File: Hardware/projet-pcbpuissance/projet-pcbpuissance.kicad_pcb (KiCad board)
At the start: 2 copper layers, 61 x 61 mm, 32 parts, among them U1 MAX5033DUSA+, U2 MAX5033DUSA+

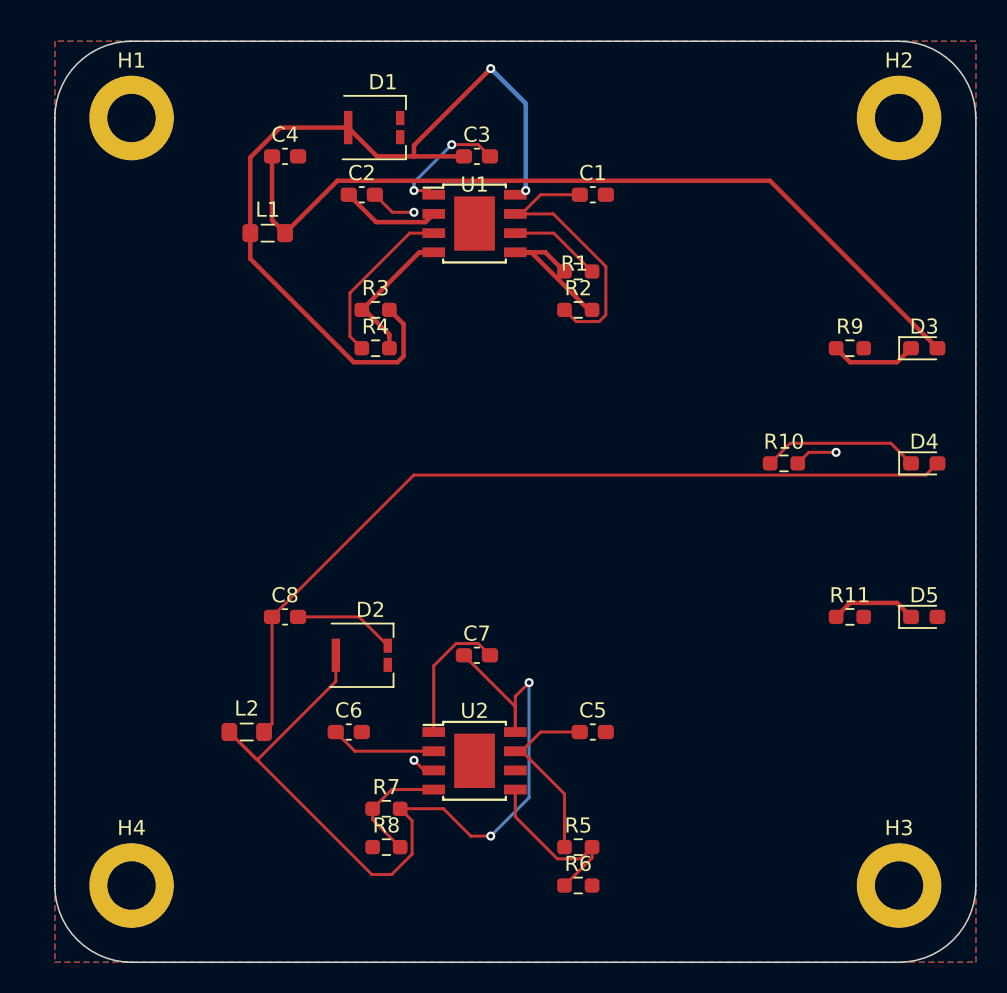
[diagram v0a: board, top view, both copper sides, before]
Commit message: Modification pcb-puissance
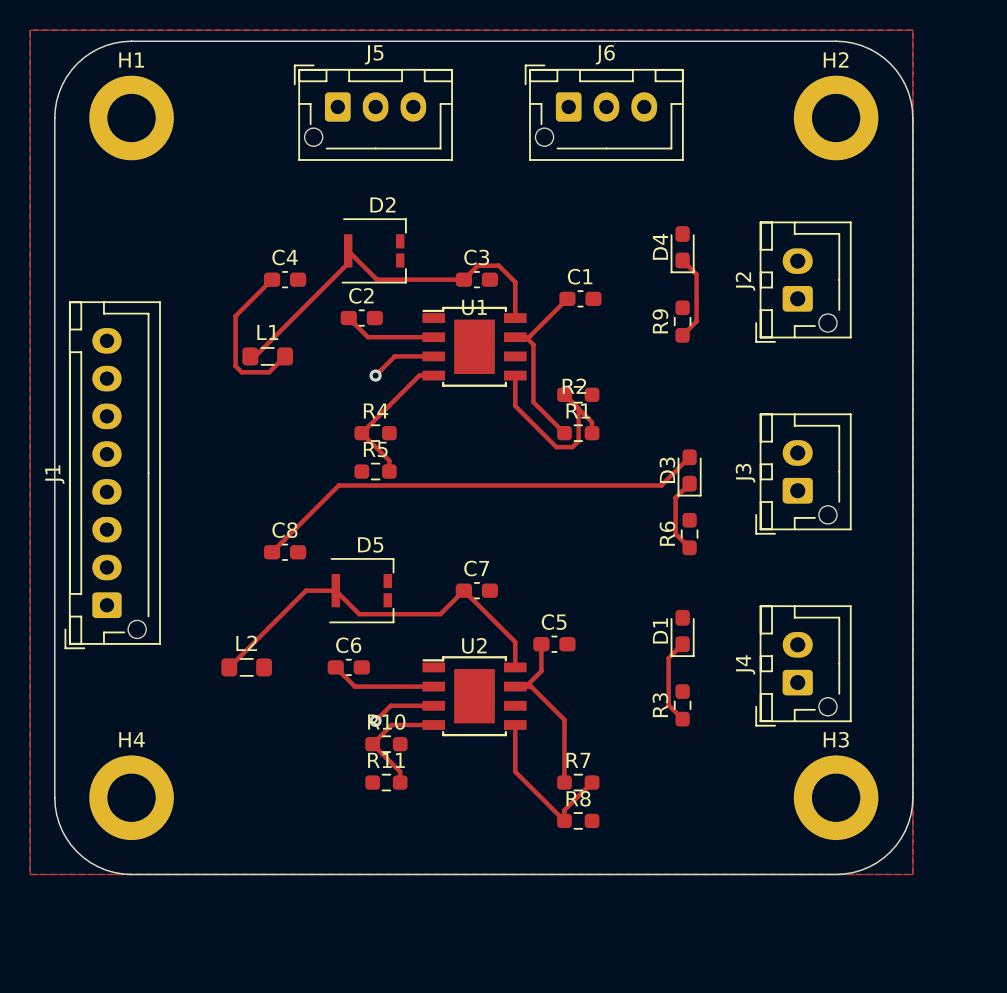
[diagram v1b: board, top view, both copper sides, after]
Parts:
- added J1: Conn_01x08, Connector_JST:JST_XH_B8B-XH-AM_1x08_P2.50mm_Vertical, F.Cu at (21.2, 60.2)
- added J2: Conn_01x02, Connector_JST:JST_XH_B2B-XH-AM_1x02_P2.50mm_Vertical, F.Cu at (67.0, 39.9)
- added J3: Conn_01x02, Connector_JST:JST_XH_B2B-XH-AM_1x02_P2.50mm_Vertical, F.Cu at (67.0, 52.6)
- added J4: Conn_01x02, Connector_JST:JST_XH_B2B-XH-AM_1x02_P2.50mm_Vertical, F.Cu at (67.0, 65.3)
- added J5: Conn_01x03, Connector_JST:JST_XH_B3B-XH-AM_1x03_P2.50mm_Vertical, F.Cu at (36.5, 27.2)
- added J6: Conn_01x03, Connector_JST:JST_XH_B3B-XH-AM_1x03_P2.50mm_Vertical, F.Cu at (51.8, 27.2)
- R1: renamed from R2; value 4,7M -> R_Small
- R2: renamed from R1; value 820k -> R_Small
- R7: renamed from R5; value 4,7M -> R_Small
- R8: renamed from R6; value 820k -> R_Small
- moved D4 29.2 mm to (59.3, 36.5), turned to 90 degrees
- moved R3 26.1 mm to (59.3, 66.8), turned to 90 degrees
- moved D1 24.6 mm to (59.3, 61.9), turned to 90 degrees
- moved R9 22.5 mm to (59.3, 41.4), turned to 90 degrees
- moved D3 15.5 mm to (59.8, 51.3), turned to 90 degrees
- moved R5 8.16 mm to (39.0, 51.3)
- moved U1 8.16 mm to (45.6, 43.1)
- moved C3 8.16 mm to (45.7, 38.6)
- moved C4 8.16 mm to (33.0, 38.6)
- moved D2 8.16 mm to (38.9, 36.7)
- moved C2 8.16 mm to (38.1, 41.2)
- moved L1 8.16 mm to (31.9, 43.7)
- moved R1 8.16 mm to (52.4, 48.8)
- moved R2 8.16 mm to (52.4, 46.3)
- moved R4 8.16 mm to (39.0, 48.8)
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- renumbered D3 to D1, D1 to D2, D4 to D3, D5 to D4, D2 to D5, R7 to R10, R8 to R11, R9 to R3, R3 to R4, R4 to R5, R10 to R6, R11 to R9
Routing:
- net +3.3V: track 54.6 -> 10.6 mm
- net Net-(D5-K): track 59.6 -> 25.4 mm, vias 2 -> 0
- net Net-(D2-K): track 57.3 -> 24.9 mm, vias 2 -> 0
- net 7.4V: track 56.1 -> 30.2 mm
- net GND: track 31.9 -> 8.64 mm, vias 3 -> 2
- net Net-(U2-BST): track 9.03 -> 0.00 mm
- net Net-(U1-BST): track 8.35 -> 0.00 mm, vias 2 -> 0
- net Batterie 11.1 V: track 31.4 -> 24.9 mm
- net Net-(D3-K): track 10.4 -> 5.01 mm
- net Net-(U1-ON/~{OFF}): track 10.4 -> 14.2 mm
- net Net-(U1-VD): track 7.38 -> 6.15 mm
- net Net-(U2-ON/~{OFF}): track 11.7 -> 11.0 mm
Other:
- board size 61 x 61 mm -> 56.8 x 55.2 mm

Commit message: Modif
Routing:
- net +3.3V: track 10.6 -> 47.3 mm, vias 0 -> 2
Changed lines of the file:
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@@
   (segment (start 59.3325 67.7275) (end 58.4075 66.8025) (width 0.3) (layer "F.Cu") (net 4))
   (segment (start 33.02 43.72) (end 31.97 44.77) (width 0.3) (layer "F.Cu") (net 6))
+  (segment (start 59.3325 61.02) (end 57.5825 61.02) (width 0.3) (layer "F.Cu") (net 6))
   (segment (start 30.155051 44.77) (end 29.745 44.359949) (width 0.3) (layer "F.Cu") (net 6))
   (segment (start 29.745 41.0525) (end 32.1575 38.64) (width 0.3) (layer "F.Cu") (net 6))
+  (segment (start 33.9325 50.07) (end 33.9325 44.6325) (width 0.3) (layer "F.Cu") (net 6))
+  (segment (start 57.5825 61.02) (end 51.7125 55.15) (width 0.3) (layer "F.Cu") (net 6))
   (segment (start 31.97 44.77) (end 30.155051 44.77) (width 0.3) (layer "F.Cu") (net 6))
+  (segment (start 33.9325 44.6325) (end 33.02 43.72) (width 0.3) (layer "F.Cu") (net 6))
   (segment (start 29.745 44.359949) (end 29.745 41.0525) (width 0.3) (layer "F.Cu") (net 6))
+  (via (at 33.9325 50.07) (size 0.8) (drill 0.4) (layers "F.Cu" "B.Cu") (net 6))
+  (via (at 51.7125 55.15) (size 0.8) (drill 0.4) (layers "F.Cu" "B.Cu") (net 6))
+  (segment (start 41.5525 55.15) (end 39.0125 55.15) (width 0.3) (layer "B.Cu") (net 6))
+  (segment (start 39.0125 55.15) (end 33.9325 50.07) (width 0.3) (layer "B.Cu") (net 6))
+  (segment (start 51.7125 55.15) (end 41.5525 55.15) (width 0.3) (layer "B.Cu") (net 6))
   (segment (start 36.375 64.305) (end 37.645 65.575) (width 0.3) (layer "F.Cu") (net 7))
   (segment (start 37.645 65.575) (end 42.86 65.575) (width 0.3) (layer "F.Cu") (net 7))

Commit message: Modification pcb puissance
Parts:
- removed J1: Conn_01x08, Connector_JST:JST_XH_B8B-XH-AM_1x08_P2.50mm_Vertical
- removed J5, J6: Conn_01x03, Connector_JST:JST_XH_B3B-XH-AM_1x03_P2.50mm_Vertical
- moved J2 18.3 mm to (51.7, 29.7), turned to 180 degrees
- moved H1 8.72 mm to (31.4, 29.8)
- moved H4 8.53 mm to (31.4, 72.9)
- moved J3 7.66 mm to (67.0, 45.0)
- moved H2 1.81 mm to (69.5, 29.8)
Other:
- board size 56.8 x 55.2 mm -> 48.3 x 53.3 mm

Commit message: Modif pcb-puissance
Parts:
- moved R6 26.5 mm to (33.9, 49.8)
- moved D3 26.4 mm to (33.9, 45.9)
- moved D4 16.5 mm to (67.0, 51.1)
- moved R9 16.5 mm to (67.0, 56.1)
- moved C1 7.38 mm to (59.4, 42.7)
- moved C2 7.38 mm to (44.9, 44.0)
- moved C3 7.38 mm to (52.5, 41.4)
- moved D2 7.38 mm to (45.7, 39.5)
- moved R1 7.38 mm to (59.3, 51.6)
- moved R2 7.38 mm to (59.3, 49.1)
- moved R4 7.38 mm to (45.8, 51.6)
- moved R5 7.38 mm to (45.8, 54.1)
- moved U1 7.38 mm to (52.4, 45.9)
- moved L1 7.38 mm to (38.7, 46.5)
- moved C4 7.38 mm to (39.8, 41.4)
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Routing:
- net Net-(D2-K): track 24.9 -> 44.8 mm, vias 0 -> 2
- net 7.4V: track 30.2 -> 21.3 mm
- net +3.3V: track 47.3 -> 41.6 mm
- net Net-(D5-K): track 25.4 -> 22.8 mm
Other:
- board size 48.3 x 53.3 mm -> 43.2 x 50.8 mm

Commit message: Modif pcb puissance
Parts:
- moved R9 27.4 mm to (53.3, 32.3), turned to 180 degrees
- moved D4 27.1 mm to (47.5, 32.3), turned to 180 degrees
- moved J2 18.9 mm to (67.0, 43.4), turned to 90 degrees
- moved J3 7.62 mm to (67.0, 52.6)
- moved D1 4.18 mm to (56.8, 58.6)
- moved R3 4.18 mm to (56.8, 63.5)
- moved J4 2.58 mm to (67.0, 62.7)
- moved H3 2.54 mm to (67.0, 70.4)
- moved H4 2.54 mm to (33.9, 70.4)
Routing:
- net +3.3V: track 41.6 -> 36.2 mm
- net Net-(D4-K): track 5.72 -> 6.64 mm
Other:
- board size 43.2 x 50.8 mm -> 43.2 x 48.3 mm

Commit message: Modif pcb puisance
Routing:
- net Batterie 11.1 V: track 24.9 -> 46.6 mm, vias 0 -> 2
- net Net-(D5-K): track 22.8 -> 37.2 mm, vias 0 -> 2
- net GND: track 8.64 -> 21.8 mm, vias 2 -> 6
- net Net-(U2-BST): track 0.00 -> 11.2 mm, vias 0 -> 2
- net Net-(U1-BST): track 0.00 -> 4.77 mm
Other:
- outline, holes or cut-outs redrawn
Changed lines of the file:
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@@
   (gr_arc (start 33.9325 75.372263) (mid 30.409508 73.912992) (end 28.950237 70.39)
     (stroke (width 0.1) (type default)) (layer "Edge.Cuts"))
-  (gr_line (start 28.950237 72.93) (end 28.8525 32.29)
+  (gr_line (start 28.950237 70.39) (end 28.8525 32.29)
     (stroke (width 0.1) (type default)) (layer "Edge.Cuts"))
   (gr_arc (start 66.9525 27.21) (mid 70.544602 28.697898) (end 72.0325 32.29)
@@
   (gr_line (start 72.0325 32.29) (end 72.0325 70.39)
     (stroke (width 0.1) (type default)) (layer "Edge.Cuts"))
-  (gr_line (start 31.3925 27.21) (end 66.9525 27.21)
+  (gr_line (start 33.9325 27.21) (end 66.9525 27.21)
     (stroke (width 0.1) (type default)) (layer "Edge.Cuts"))
   (gr_arc (start 28.8525 32.29) (mid 30.340398 28.697898) (end 33.9325 27.21)
@@
   (segment (start 56.2875 45.75) (end 56.2875 49.55) (width 0.3) (layer "F.Cu") (net 1))
   (segment (start 49.31 63.035) (end 48.26 63.035) (width 0.3) (layer "F.Cu") (net 1))
+  (segment (start 59.3325 47.53) (end 57.0575 45.255) (width 0.3) (layer "F.Cu") (net 1))
   (segment (start 48.965 63.035) (end 48.26 63.035) (width 0.3) (layer "F.Cu") (net 1))
+  (segment (start 51.7125 58.505) (end 51.7125 57.69) (width 0.3) (layer "F.Cu") (net 1))
   (segment (start 51.515 69.385) (end 51.515 65.24) (width 0.3) (layer "F.Cu") (net 1))
   (segment (start 51.515 65.24) (end 49.31 63.035) (width 0.3) (layer "F.Cu") (net 1))
+  (segment (start 57.0575 45.255) (end 55.0875 45.255) (width 0.3) (layer "F.Cu") (net 1))
+  (segment (start 49.9875 60.23) (end 51.7125 58.505) (width 0.3) (layer "F.Cu") (net 1))
   (segment (start 49.9875 62.0125) (end 48.965 63.035) (width 0.3) (layer "F.Cu") (net 1))
   (segment (start 58.54 42.715) (end 56 45.255) (width 0.3) (layer "F.Cu") (net 1))
@@
   (segment (start 55.0875 45.255) (end 55.7925 45.255) (width 0.3) (layer "F.Cu") (net 1))
   (segment (start 56.2875 49.55) (end 58.3425 51.605) (width 0.3) (layer "F.Cu") (net 1))
+  (via (at 51.7125 57.69) (size 0.8) (drill 0.4) (layers "F.Cu" "B.Cu") (net 1))
+  (via (at 59.3325 47.53) (size 0.8) (drill 0.4) (layers "F.Cu" "B.Cu") (net 1))
+  (segment (start 51.7125 57.69) (end 59.3325 50.07) (width 0.3) (layer "B.Cu") (net 1))
+  (segment (start 59.3325 50.07) (end 59.3325 47.53) (width 0.3) (layer "B.Cu") (net 1))
   (segment (start 40.0175 64.305) (end 39.0125 65.31) (width 0.3) (layer "F.Cu") (net 2))
+  (segment (start 48.26 64.305) (end 48.704502 64.305) (width 0.3) (layer "F.Cu") (net 2))
   (segment (start 49.6875 46.525) (end 47.11 46.525) (width 0.3) (layer "F.Cu") (net 2))
+  (segment (start 60.1675 49.065) (end 60.3375 49.065) (width 0.3) (layer "F.Cu") (net 2))
+  (segment (start 60.3375 49.065) (end 61.8725 47.53) (width 0.3) (layer "F.Cu") (net 2))
   (segment (start 42.86 64.305) (end 40.0175 64.305) (width 0.3) (layer "F.Cu") (net 2))
+  (segment (start 35.11 50.07) (end 36.4725 50.07) (width 0.3) (layer "F.Cu") (net 2))
+  (segment (start 48.704502 64.305) (end 49.709502 65.31) (width 0.3) (layer "F.Cu") (net 2))
+  (segment (start 51.7125 62.77) (end 51.7125 60.23) (width 0.3) (layer "F.Cu") (net 2))
   (segment (start 47.11 46.525) (end 45.84 47.795) (width 0.3) (layer "F.Cu") (net 2))
+  (segment (start 33.9325 48.8925) (end 35.11 50.07) (width 0.3) (layer "F.Cu") (net 2))
+  (via (at 51.7125 62.77) (size 0.8) (drill 0.4) (layers "F.Cu" "B.Cu") (net 2))
+  (via (at 36.4725 50.07) (size 0.8) (drill 0.4) (layers "F.Cu" "B.Cu") (free) (net 2))
+  (via (at 61.8725 47.53) (size 0.8) (drill 0.4) (layers "F.Cu" "B.Cu") (free) (net 2))
   (via (at 45.84 47.795) (size 0.8) (drill 0.4) (layers "F.Cu" "B.Cu") (free) (net 2))
+  (via (at 49.709502 65.31) (size 0.8) (drill 0.4) (layers "F.Cu" "B.Cu") (net 2))
   (via (at 39.0125 65.31) (size 0.8) (drill 0.4) (layers "F.Cu" "B.Cu") (free) (net 2))
+  (segment (start 49.709502 65.31) (end 49.709502 64.772998) (width 0.3) (layer "B.Cu") (net 2))
+  (segment (start 49.709502 64.772998) (end 51.7125 62.77) (width 0.3) (layer "B.Cu") (net 2))
   (segment (start 44.065 43.985) (end 45.335 45.255) (width 0.3) (layer "F.Cu") (net 3))
   (segment (start 45.335 45.255) (end 49.6875 45.255) (width 0.3) (layer "F.Cu") (net 3))
@@
   (segment (start 55.8675 60.37) (end 56.7925 59.445) (width 0.3) (layer "F.Cu") (net 4))
   (segment (start 56.7925 64.4025) (end 55.8675 63.4775) (width 0.3) (layer "F.Cu") (net 4))
+  (segment (start 49.6875 43.985) (end 51.3025 42.37) (width 0.3) (layer "F.Cu") (net 5))
+  (segment (start 51.3025 42.37) (end 52.485 42.37) (width 0.3) (layer "F.Cu") (net 5))
+  (segment (start 52.485 42.37) (end 53.41 41.445) (width 0.3) (layer "F.Cu") (net 5))
   (segment (start 39.8475 46.525) (end 38.7975 47.575) (width 0.3) (layer "F.Cu") (net 6))
   (segment (start 56.7925 57.695) (end 55.0425 57.695) (width 0.3) (layer "F.Cu") (net 6))
@@
   (segment (start 44.143516 50.07) (end 41.6095 47.535984) (width 0.3) (layer "B.Cu") (net 8))
   (segment (start 49.1725 50.07) (end 44.143516 50.07) (width 0.3) (layer "B.Cu") (net 8))
+  (segment (start 42.86 61.765) (end 42.86 61.4625) (width 0.3) (layer "F.Cu") (net 9))
+  (segment (start 49.1725 57.69) (end 47.5875 57.69) (width 0.3) (layer "F.Cu") (net 9))
+  (segment (start 42.86 61.4625) (end 44.0925 60.23) (width 0.3) (layer "F.Cu") (net 9))
+  (segment (start 47.5875 57.69) (end 46.5825 56.685) (width 0.3) (layer "F.Cu") (net 9))
+  (via (at 44.0925 60.23) (size 0.8) (drill 0.4) (layers "F.Cu" "B.Cu") (net 9))
+  (via (at 49.1725 57.69) (size 0.8) (drill 0.4) (layers "F.Cu" "B.Cu") (net 9))
+  (segment (start 44.0925 60.23) (end 46.6325 57.69) (width 0.3) (layer "B.Cu") (net 9))
+  (segment (start 46.6325 57.69) (end 49.1725 57.69) (width 0.3) (layer "B.Cu") (net 9))
   (segment (start 30.4175 58.425) (end 32.1575 56.685) (width 0.3) (layer "F.Cu") (net 10))
   (segment (start 33.6925 60.23) (end 32.6425 61.28) (width 0.3) (layer "F.Cu") (net 10))
@@
   (segment (start 49.3075 31.365) (end 53.3275 31.365) (width 0.3) (layer "F.Cu") (net 12))
   (segment (start 35.455 57.61) (end 36.38 56.685) (width 0.3) (layer "F.Cu") (net 13))
-  (segment (start 37.935 58.24) (end 43.3025 58.24) (width 0.3) (layer "F.Cu") (net 13))
+  (segment (start 40.64 66.845) (end 41.645 67.85) (width 0.3) (layer "F.Cu") (net 13))
+  (segment (start 36.38 56.685) (end 37.935 58.24) (width 0.3) (layer "F.Cu") (net 13))
+  (segment (start 41.645 67.85) (end 44.0925 67.85) (width 0.3) (layer "F.Cu") (net 13))
+  (segment (start 41.5525 60.23) (end 41.5525 58.24) (width 0.3) (layer "F.Cu") (net 13))
   (segment (start 31.3925 60.23) (end 34.0125 57.61) (width 0.3) (layer "F.Cu") (net 13))
   (segment (start 34.0125 57.61) (end 35.455 57.61) (width 0.3) (layer "F.Cu") (net 13))
   (segment (start 44.8575 56.685) (end 48.26 60.0875) (width 0.3) (layer "F.Cu") (net 13))
-  (segment (start 36.38 56.685) (end 37.935 58.24) (width 0.3) (layer "F.Cu") (net 13))
-  (segment (start 34.0125 57.61) (end 33.9325 57.69) (width 0.3) (layer "F.Cu") (net 13))
+  (segment (start 37.935 58.24) (end 41.5525 58.24) (width 0.3) (layer "F.Cu") (net 13))
+  (segment (start 41.5525 58.24) (end 43.3025 58.24) (width 0.3) (layer "F.Cu") (net 13))
   (segment (start 43.3025 58.24) (end 44.8575 56.685) (width 0.3) (layer "F.Cu") (net 13))
   (segment (start 48.26 60.0875) (end 48.26 61.765) (width 0.3) (layer "F.Cu") (net 13))
+  (via (at 41.5525 60.23) (size 0.8) (drill 0.4) (layers "F.Cu" "B.Cu") (net 13))
+  (via (at 44.0925 67.85) (size 0.8) (drill 0.4) (layers "F.Cu" "B.Cu") (net 13))
+  (segment (start 44.0925 62.77) (end 41.5525 60.23) (width 0.3) (layer "B.Cu") (net 13))
+  (segment (start 44.0925 67.85) (end 44.0925 62.77) (width 0.3) (layer "B.Cu") (net 13))
   (segment (start 58.3425 49.065) (end 59.28 50.0025) (width 0.3) (layer "F.Cu") (net 15))
   (segment (start 60.1675 50.89) (end 58.3425 49.065) (width 0.3) (layer "F.Cu") (net 15))

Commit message: Modif
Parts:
- removed D5: D_Zener, Diode_SMD:Littelfuse_PolyZen-LS
- added D6: D_Schottky, Diode_THT:D_DO-201AD_P12.70mm_Horizontal, F.Cu at (76.6, 24.2)
- C1, C4, C5, C8: footprint Capacitor_SMD:C_0603_1608Metric_Pad1.08x0.95mm_HandSolder -> Capacitor_SMD:CP_Elec_6.3x7.7
- D2: value D_Zener -> D_Schottky; footprint Diode_SMD:Littelfuse_PolyZen-LS -> Diode_THT:D_DO-201AD_P12.70mm_Horizontal
- L1, L2: footprint Inductor_SMD:L_0805_2012Metric_Pad1.05x1.20mm_HandSolder -> Inductor_SMD:L_12x12mm_H6mm
- moved H4 56.2 mm to (87.3, 52.6)
- moved H1 53.4 mm to (87.3, 31.2)
- moved D3 43.5 mm to (76.5, 54.9), turned to 0 degrees
- moved C8 38.7 mm to (69.0, 42.6)
- moved D4 38.4 mm to (76.5, 57.5), turned to 0 degrees
- moved D2 38.0 mm to (76.6, 17.5)
- moved L2 34.4 mm to (56.4, 35.5)
- moved C4 32.9 mm to (69.0, 26.3)
- moved H3 32.2 mm to (87.3, 45.5)
- moved C5 31.5 mm to (69.0, 34.5)
- moved L1 30.9 mm to (56.4, 21.2)
- moved R8 26.6 mm to (59.9, 46.4)
- moved R7 26.6 mm to (59.9, 43.8)
- moved C1 26.4 mm to (69.0, 18.2)
- moved R11 25.4 mm to (59.9, 53.9)
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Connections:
- C3 pad 1: Net-(D2-K) -> Net-(D6-K)
- C7 pad 1: Net-(D5-K) -> Net-(D2-K)
- J2 pad 1: VCC -> Batterie 11.1 V
- J3 pad 1: VCC -> Batterie 11.1 V
- J4 pad 1: VCC -> Batterie 11.1 V
- L1 pad 1: Net-(D2-K) -> Net-(D6-K)
- L2 pad 1: Net-(D5-K) -> Net-(D2-K)
- R10 pad 2: Net-(D5-K) -> Net-(D2-K)
- R4 pad 2: Net-(D2-K) -> Net-(D6-K)
- U1 pad 8: Net-(D2-K) -> Net-(D6-K)
- U2 pad 8: Net-(D5-K) -> Net-(D2-K)
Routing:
- net Batterie 11.1 V: track 46.6 -> 0.00 mm, vias 2 -> 0
- net Net-(D2-K): track 44.8 -> 0.00 mm, vias 2 -> 0
- net Net-(D5-K): track 37.2 -> 0.00 mm, vias 2 -> 0
- net +3.3V: track 36.2 -> 0.00 mm, vias 2 -> 0
- net GND: track 21.8 -> 0.00 mm, vias 6 -> 0
- net 7.4V: track 21.3 -> 0.00 mm
- net Net-(U1-ON/~{OFF}): track 14.2 -> 0.00 mm
- net Net-(U2-BST): track 11.2 -> 0.00 mm, vias 2 -> 0
- net Net-(U2-ON/~{OFF}): track 11.0 -> 0.00 mm
- net Net-(U1-FB): track 9.63 -> 0.00 mm
- net Net-(U2-FB): track 7.87 -> 0.00 mm
- net Net-(U2-VD): track 7.01 -> 0.00 mm
- net Net-(D4-K): track 6.64 -> 0.00 mm
- net Net-(U1-VD): track 6.15 -> 0.00 mm
- net Net-(D1-K): track 5.72 -> 0.00 mm
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- removed copper zone on B.Cu, net GND
- removed copper zone on F.Cu, net GND
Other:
- board outline removed

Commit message: Modif
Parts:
- moved H2 110.7 mm to (166.0, 116.1)
- moved L2 99.7 mm to (131.6, 100.9)
- moved J4 99.4 mm to (160.9, 100.9)
- moved L1 96.9 mm to (133.0, 80.5)
- moved J3 96.7 mm to (160.9, 88.0)
- moved C8 96.3 mm to (145.7, 100.9)
- moved C4 95.0 mm to (147.0, 80.5)
- moved D2 94.7 mm to (121.6, 100.9), turned to 180 degrees
- moved J2 94.4 mm to (160.9, 75.5)
- moved R9 94.2 mm to (151.0, 72.9), turned to 180 degrees
- moved C5 88.1 mm to (112.7, 111.0), turned to -90 degrees
- moved R6 86.1 mm to (132.1, 93.2), turned to 180 degrees
- moved H1 85.8 mm to (166.0, 65.3)
- moved C1 85.3 mm to (113.9, 90.7), turned to -90 degrees
- moved R7 83.7 mm to (107.6, 112.7), turned to -90 degrees
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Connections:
- D4 pad 2: 11.1V -> Batterie 11.1 V
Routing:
- net Batterie 11.1 V: track 0.00 -> 104.1 mm
- net Net-(D2-K): track 0.00 -> 32.4 mm
- net Net-(D6-K): track 0.00 -> 30.2 mm
- net Net-(U2-FB): track 0.00 -> 16.8 mm
- net Net-(U1-FB): track 0.00 -> 15.7 mm
- net 7.4V: track 0.00 -> 15.1 mm
- net +3.3V: track 0.00 -> 15.0 mm
- net Net-(U1-ON/~{OFF}): track 0.00 -> 7.13 mm
- net Net-(U2-ON/~{OFF}): track 0.00 -> 6.29 mm
- net Net-(U2-VD): track 0.00 -> 3.88 mm
- net Net-(U2-BST): track 0.00 -> 3.59 mm
- net Net-(U1-VD): track 0.00 -> 3.52 mm
- net Net-(D1-K): track 0.00 -> 3.33 mm
- net Net-(D3-K): track 0.00 -> 3.33 mm
- net Net-(U1-BST): track 0.00 -> 2.66 mm
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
